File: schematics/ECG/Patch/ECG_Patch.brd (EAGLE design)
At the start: 27.3 x 27.3 mm, 7 parts

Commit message: changed 4 pin to through hole and added v1.0 marking
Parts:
- removed U$1: M80-4SMT, harwin:M80-4_SMT
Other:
- board text added: "ECG Patch v1.0"
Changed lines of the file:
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@@
 <setting verticaltext="up"/>
 </settings>
-<grid distance="1" unitdist="mil" unit="mil" style="lines" multiple="1" display="no" altdistance="0.025" altunitdist="inch" altunit="inch"/>
+<grid distance="0.001" unitdist="inch" unit="inch" style="lines" multiple="1" display="yes" altdistance="0.025" altunitdist="inch" altunit="inch"/>
 <layers>
 <layer number="1" name="Top" color="4" fill="1" visible="yes" active="yes"/>
@@
 <wire x1="27.305" y1="27.305" x2="0" y2="27.305" width="0" layer="20"/>
 <wire x1="0" y1="27.305" x2="0" y2="0" width="0" layer="20"/>
-<circle x="26.797" y="13.208" radius="0.08031875" width="0.4064" layer="21"/>
+<circle x="21.4122" y="13.2588" radius="0.508" width="0.4064" layer="22"/>
+<text x="22.8092" y="26.3652" size="0.4064" layer="21">ECG Patch v1.0</text>
 </plain>
 <attributes>
@@
 </autorouter>
 <elements>
-<element name="CONN1" library="harwin" package="M80-4-V" value="M80-4V" x="2.667" y="13.2588"/>
 <element name="CONN2" library="harwin" package="M80-6-V" value="M80-6V" x="24.638" y="13.2588" rot="R90"/>
 <element name="LL" library="testpad" package="TP20R" value="TPTP20R" x="22.86" y="8.001" rot="MR270">
@@
 <attribute name="TP_SIGNAL_NAME" value="" x="18.5674" y="18.542" size="1.778" layer="28" rot="MR270" display="off"/>
 </element>
-<element name="U$1" library="harwin" package="M80-4_SMT" value="M80-4SMT" x="11.8618" y="13.2842" rot="R90"/>
+<element name="CONN1" library="harwin" package="M80-4-V" value="M80-4V" x="2.667" y="13.2588"/>
 </elements>
 <signals>

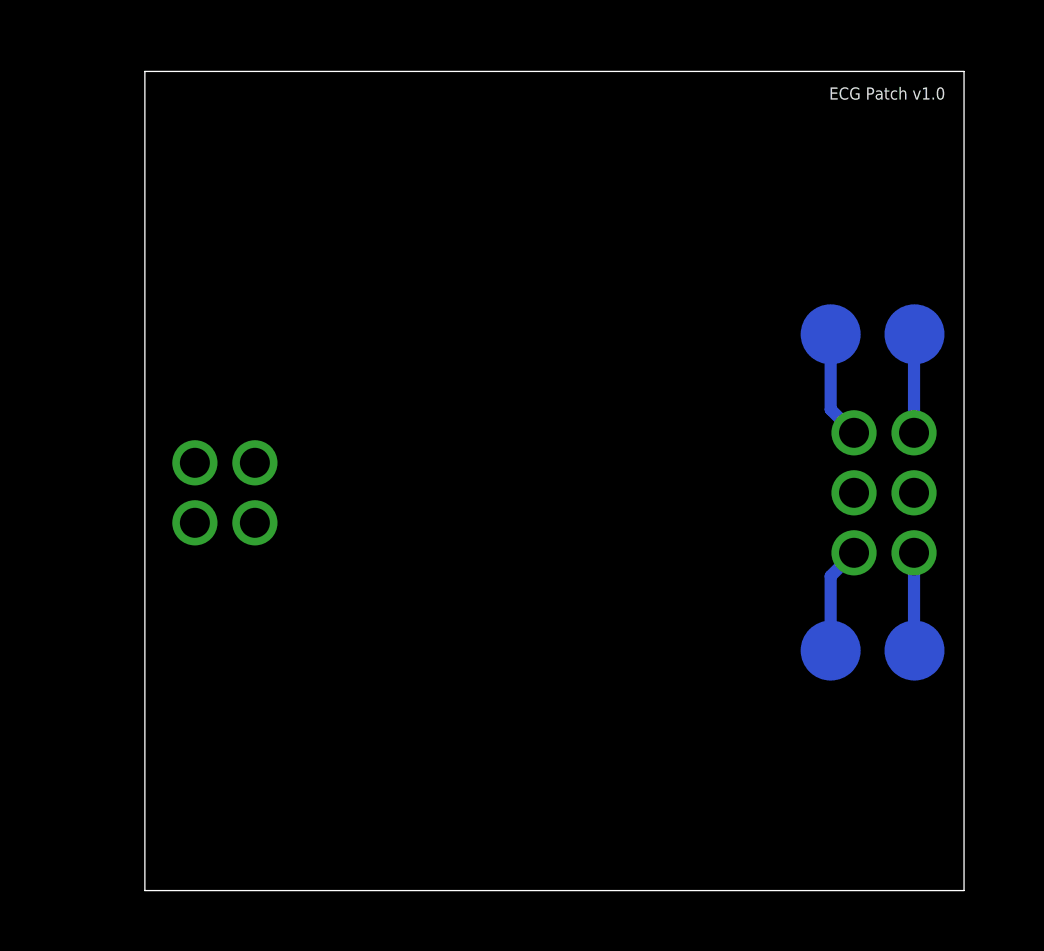
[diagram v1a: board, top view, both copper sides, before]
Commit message: switched ECG boards to spring loaded pin headers
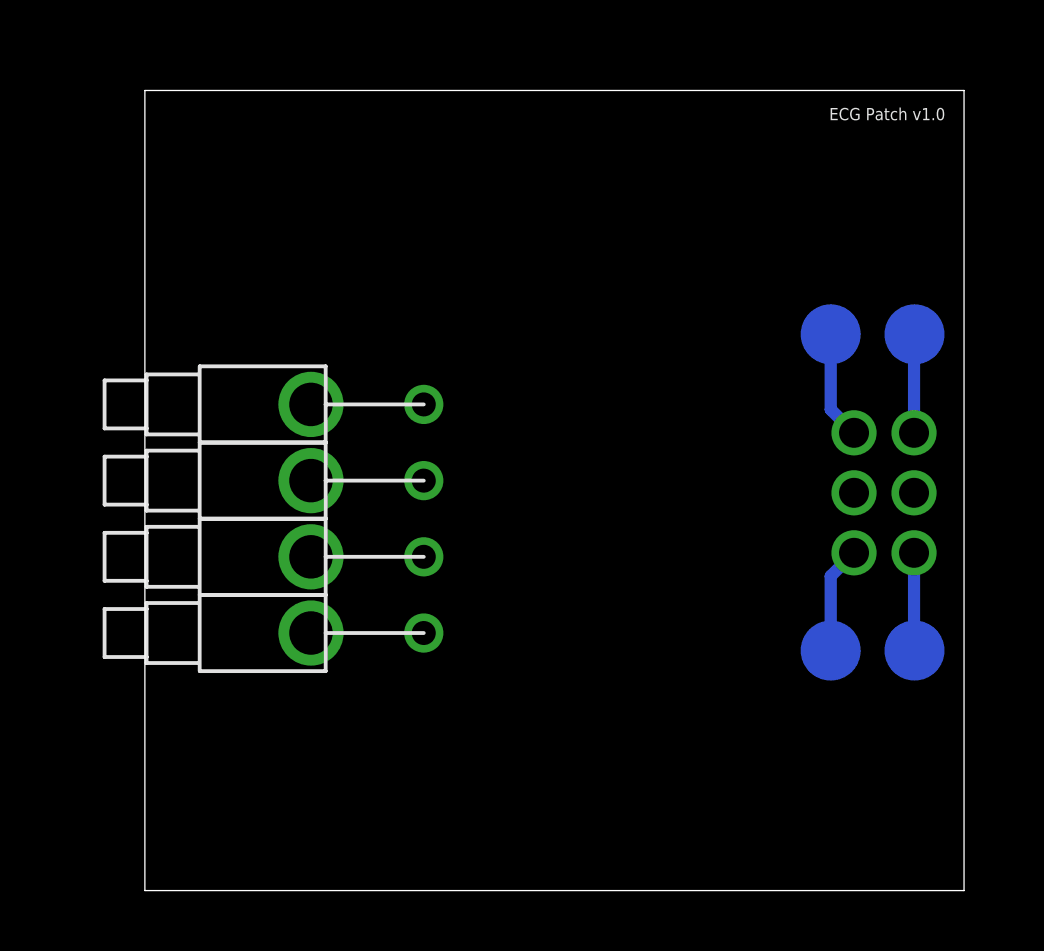
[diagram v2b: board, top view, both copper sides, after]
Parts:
- removed CONN1: M80-4V, harwin:M80-4-V
- added U$1, U$2, U$3, U$4: PISTON_RA_TH, pins:PISTON_RA_TH
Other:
- board size 27.3 x 27.3 mm -> 27.3 x 26.7 mm
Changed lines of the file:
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@@
 <?xml version="1.0" encoding="utf-8"?>
 <!DOCTYPE eagle SYSTEM "eagle.dtd">
-<eagle version="6.4">
+<eagle version="6.5.0">
 <drawing>
 <settings>
@@
 <plain>
 <wire x1="0" y1="0" x2="27.305" y2="0" width="0" layer="20"/>
-<wire x1="27.305" y1="0" x2="27.305" y2="27.305" width="0" layer="20"/>
-<wire x1="27.305" y1="27.305" x2="0" y2="27.305" width="0" layer="20"/>
-<wire x1="0" y1="27.305" x2="0" y2="0" width="0" layer="20"/>
+<wire x1="27.305" y1="0" x2="27.305" y2="26.67" width="0" layer="20"/>
+<wire x1="27.305" y1="26.67" x2="0" y2="26.67" width="0" layer="20"/>
+<wire x1="0" y1="26.67" x2="0" y2="0" width="0" layer="20"/>
 <circle x="21.4122" y="13.2588" radius="0.508" width="0.4064" layer="22"/>
-<text x="22.8092" y="26.3652" size="0.4064" layer="21">ECG Patch v1.0</text>
+<text x="22.8092" y="25.6794" size="0.4064" layer="21">ECG Patch v1.0</text>
 </plain>
 <attributes>
@@
 <attribute name="TP_SIGNAL_NAME" value="" x="18.5674" y="18.542" size="1.778" layer="28" rot="MR270" display="off"/>
 </element>
-<element name="CONN1" library="harwin" package="M80-4-V" value="M80-4V" x="2.667" y="13.2588"/>
+<element name="U$1" library="pins" package="PISTON_RA_TH" value="PISTON_RA_TH" x="9.2964" y="16.2052" rot="R180"/>
+<element name="U$2" library="pins" package="PISTON_RA_TH" value="PISTON_RA_TH" x="9.2964" y="13.6652" rot="R180"/>
+<element name="U$3" library="pins" package="PISTON_RA_TH" value="PISTON_RA_TH" x="9.2964" y="11.1252" rot="R180"/>
+<element name="U$4" library="pins" package="PISTON_RA_TH" value="PISTON_RA_TH" x="9.2964" y="8.5852" rot="R180"/>
 </elements>
 <signals>

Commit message: redesigned patch board and charging board
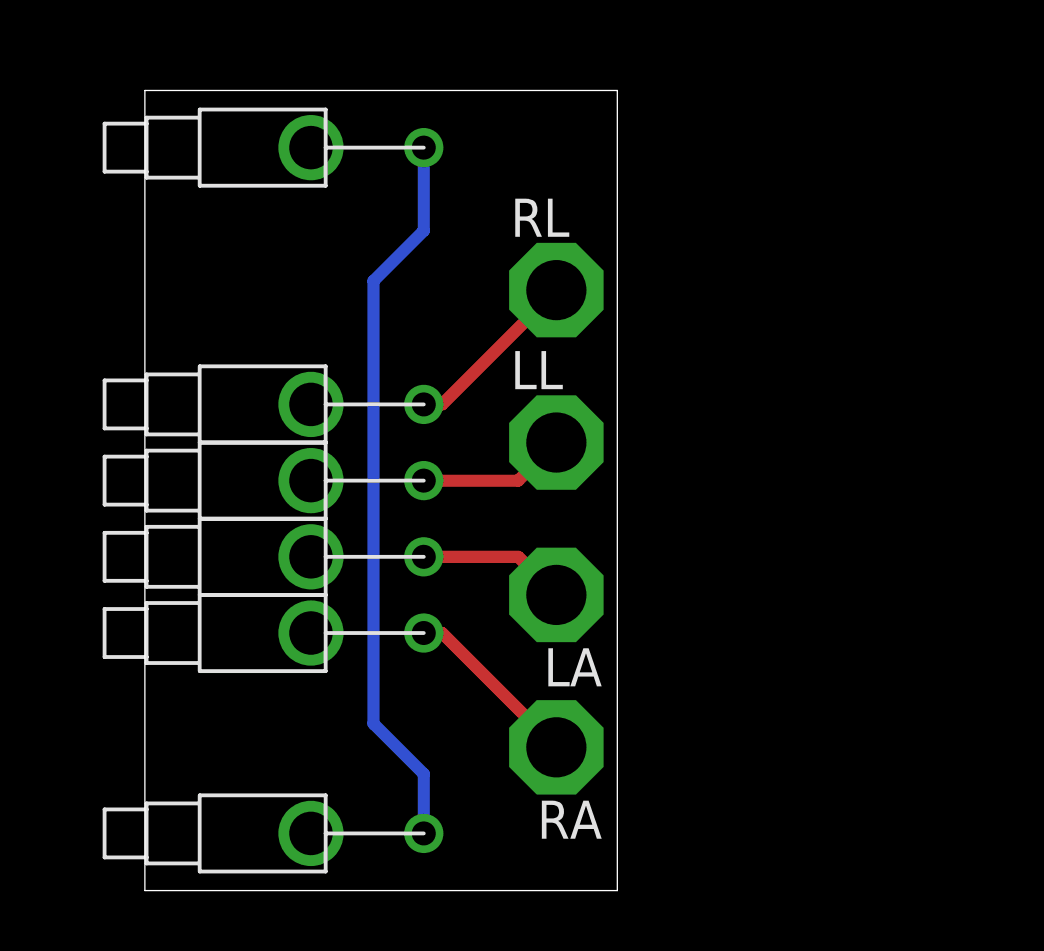
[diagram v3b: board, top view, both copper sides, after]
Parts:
- removed CONN2: M80-6V, harwin:M80-6-V
- added U$5, U$6: PISTON_RA_TH, pins:PISTON_RA_TH
- LA, LL, RA, RL: value TPTP20R -> TPSQPAD1-20; device testpad:TP20R -> testpad:P1-20
- moved RA 18.2 mm to (13.7, 4.78), flipped to the top, turned to 180 degrees
- moved LA 12.1 mm to (13.7, 9.86), flipped to the top
- moved LL 11.5 mm to (13.7, 14.9), flipped to the top, turned to 0 degrees
- moved RL 9.26 mm to (13.7, 20.0), flipped to the top, turned to 0 degrees
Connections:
- removed net LA: CONN2.1, LA.TP
- removed net LL: CONN2.6, LL.TP
- removed net RA: CONN2.3, RA.TP
- removed net RL: CONN2.4, RL.TP
- new net BATT: U$5.1, U$6.1
- new net N$1: LL.TP, U$2.1
- new net N$2: RL.TP, U$1.1
- new net N$3: LA.TP, U$3.1
- new net N$4: RA.TP, U$4.1
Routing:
- net BATT: track 0.00 -> 24.2 mm
- net N$4: track 0.00 -> 6.00 mm
- net N$2: track 0.00 -> 6.00 mm
- net N$3: track 0.00 -> 4.95 mm
- net N$1: track 0.00 -> 4.95 mm
- net RL: track 3.61 -> 0.00 mm
- net LL: track 3.58 -> 0.00 mm
- net RA: track 3.29 -> 0.00 mm
- net LA: track 3.26 -> 0.00 mm
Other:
- board size 27.3 x 26.7 mm -> 15.7 x 26.7 mm
- board text removed: "ECG Patch v1.0"
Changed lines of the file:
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@@
 <setting verticaltext="up"/>
 </settings>
-<grid distance="0.001" unitdist="inch" unit="inch" style="lines" multiple="1" display="yes" altdistance="0.025" altunitdist="inch" altunit="inch"/>
+<grid distance="0.001" unitdist="inch" unit="mil" style="lines" multiple="1" display="yes" altdistance="0.025" altunitdist="inch" altunit="inch"/>
 <layers>
 <layer number="1" name="Top" color="4" fill="1" visible="yes" active="yes"/>
-<layer number="2" name="Route2" color="1" fill="3" visible="no" active="yes"/>
+<layer number="2" name="Route2" color="1" fill="3" visible="no" active="no"/>
 <layer number="3" name="Route3" color="4" fill="3" visible="no" active="no"/>
 <layer number="14" name="Route14" color="1" fill="6" visible="no" active="no"/>
-<layer number="15" name="Route15" color="4" fill="6" visible="no" active="yes"/>
+<layer number="15" name="Route15" color="4" fill="6" visible="no" active="no"/>
 <layer number="16" name="Bottom" color="1" fill="1" visible="yes" active="yes"/>
 <layer number="17" name="Pads" color="2" fill="1" visible="yes" active="yes"/>
@@
 <board>
 <plain>
-<wire x1="0" y1="0" x2="27.305" y2="0" width="0" layer="20"/>
-<wire x1="27.305" y1="0" x2="27.305" y2="26.67" width="0" layer="20"/>
-<wire x1="27.305" y1="26.67" x2="0" y2="26.67" width="0" layer="20"/>
+<wire x1="0" y1="0" x2="15.748" y2="0" width="0" layer="20"/>
+<wire x1="15.748" y1="0" x2="15.748" y2="26.67" width="0" layer="20"/>
+<wire x1="15.748" y1="26.67" x2="0" y2="26.67" width="0" layer="20"/>
 <wire x1="0" y1="26.67" x2="0" y2="0" width="0" layer="20"/>
-<circle x="21.4122" y="13.2588" radius="0.508" width="0.4064" layer="22"/>
-<text x="22.8092" y="25.6794" size="0.4064" layer="21">ECG Patch v1.0</text>
 </plain>
 <attributes>
@@
 necessary adjustments and save your customized
 design rules under a new name.</description>
-<param name="layerSetup" value="(1*2+15*16)"/>
+<param name="layerSetup" value="(1*16)"/>
 <param name="mtCopper" value="0.035mm 0.035mm 0.035mm 0.035mm 0.035mm 0.035mm 0.035mm 0.035mm 0.035mm 0.035mm 0.035mm 0.035mm 0.035mm 0.035mm 0.035mm 0.035mm"/>
 <param name="mtIsolate" value="0.5mm 0.5mm 0.2mm 0.15mm 0.2mm 0.15mm 0.2mm 0.15mm 0.2mm 0.15mm 0.2mm 0.15mm 0.2mm 0.15mm 0.5mm"/>
@@
 </autorouter>
 <elements>
-<element name="CONN2" library="harwin" package="M80-6-V" value="M80-6V" x="24.638" y="13.2588" rot="R90"/>
-<element name="LL" library="testpad" package="TP20R" value="TPTP20R" x="22.86" y="8.001" rot="MR270">
-<attribute name="TP_SIGNAL_NAME" value="" x="22.86" y="8.001" size="1.778" layer="28" rot="MR270" display="off"/>
-</element>
-<element name="LA" library="testpad" package="TP20R" value="TPTP20R" x="25.654" y="8.001" rot="MR180">
-<attribute name="TP_SIGNAL_NAME" value="" x="25.654" y="8.001" size="1.778" layer="28" rot="MR180" display="off"/>
-</element>
-<element name="RA" library="testpad" package="TP20R" value="TPTP20R" x="25.654" y="18.542" rot="MR0">
-<attribute name="TP_SIGNAL_NAME" value="" x="25.654" y="18.542" size="1.778" layer="28" rot="MR0" display="off"/>
-</element>
-<element name="RL" library="testpad" package="TP20R" value="TPTP20R" x="22.86" y="18.542" rot="MR270">
-<attribute name="TP_SIGNAL_NAME" value="" x="18.5674" y="18.542" size="1.778" layer="28" rot="MR270" display="off"/>
-</element>
 <element name="U$1" library="pins" package="PISTON_RA_TH" value="PISTON_RA_TH" x="9.2964" y="16.2052" rot="R180"/>
 <element name="U$2" library="pins" package="PISTON_RA_TH" value="PISTON_RA_TH" x="9.2964" y="13.6652" rot="R180"/>
 <element name="U$3" library="pins" package="PISTON_RA_TH" value="PISTON_RA_TH" x="9.2964" y="11.1252" rot="R180"/>
 <element name="U$4" library="pins" package="PISTON_RA_TH" value="PISTON_RA_TH" x="9.2964" y="8.5852" rot="R180"/>
+<element name="LL" library="testpad" package="P1-20" value="TPSQPAD1-20" x="13.716" y="14.9352">
+<attribute name="TP_SIGNAL_NAME" value="" x="13.716" y="14.9352" size="1.778" layer="27" display="off"/>
+</element>
+<element name="RL" library="testpad" package="P1-20" value="TPSQPAD1-20" x="13.716" y="20.0152">
+<attribute name="TP_SIGNAL_NAME" value="" x="13.716" y="20.0152" size="1.778" layer="27" display="off"/>
+</element>
+<element name="LA" library="testpad" package="P1-20" value="TPSQPAD1-20" x="13.716" y="9.8552" rot="R180">
+<attribute name="TP_SIGNAL_NAME" value="" x="13.716" y="9.8552" size="1.778" layer="27" rot="R180" display="off"/>
+</element>
+<element name="RA" library="testpad" package="P1-20" value="TPSQPAD1-20" x="13.716" y="4.7752" rot="R180">
+<attribute name="TP_SIGNAL_NAME" value="" x="13.716" y="4.7752" size="1.778" layer="27" rot="R180" display="off"/>
+</element>
+<element name="U$5" library="pins" package="PISTON_RA_TH" value="PISTON_RA_TH" x="9.2964" y="24.765" rot="R180"/>
+<element name="U$6" library="pins" package="PISTON_RA_TH" value="PISTON_RA_TH" x="9.2964" y="1.905" rot="R180"/>
 </elements>
 <signals>
-<signal name="LA">
-<contactref element="CONN2" pad="1"/>
+<signal name="N$1">
+<contactref element="U$2" pad="1"/>
+<contactref element="LL" pad="TP"/>
+<wire x1="9.2964" y1="13.6652" x2="12.446" y2="13.6652" width="0.4064" layer="1"/>
+<wire x1="12.446" y1="13.6652" x2="13.716" y2="14.9352" width="0.4064" layer="1"/>
+</signal>
+<signal name="N$2">
+<contactref element="U$1" pad="1"/>
+<contactref element="RL" pad="TP"/>
+<wire x1="9.2964" y1="16.2052" x2="9.906" y2="16.2052" width="0.4064" layer="1"/>
+<wire x1="9.906" y1="16.2052" x2="13.716" y2="20.0152" width="0.4064" layer="1"/>
+</signal>
+<signal name="N$3">
+<contactref element="U$3" pad="1"/>
 <contactref element="LA" pad="TP"/>
-<wire x1="25.638" y1="11.2588" x2="25.638" y2="8.017" width="0.4064" layer="16"/>
-<wire x1="25.638" y1="8.017" x2="25.654" y2="8.001" width="0.4064" layer="16"/>
-</signal>
-<signal name="RL">
-<contactref element="RL" pad="TP"/>
-<contactref element="CONN2" pad="4"/>
-<wire x1="22.86" y1="18.542" x2="22.86" y2="16.0368" width="0.4064" layer="16"/>
-<wire x1="22.86" y1="16.0368" x2="23.638" y2="15.2588" width="0.4064" layer="16"/>
-</signal>
-<signal name="LL">
-<contactref element="CONN2" pad="6"/>
-<contactref element="LL" pad="TP"/>
-<wire x1="22.86" y1="8.001" x2="22.86" y2="10.4808" width="0.4064" layer="16"/>
-<wire x1="22.86" y1="10.4808" x2="23.638" y2="11.2588" width="0.4064" layer="16"/>
-</signal>
-<signal name="RA">
+<wire x1="9.2964" y1="11.1252" x2="12.446" y2="11.1252" width="0.4064" layer="1"/>
+<wire x1="12.446" y1="11.1252" x2="13.716" y2="9.8552" width="0.4064" layer="1"/>
+</signal>
+<signal name="N$4">
+<contactref element="U$4" pad="1"/>
 <contactref element="RA" pad="TP"/>
-<contactref element="CONN2" pad="3"/>
-<wire x1="25.638" y1="15.2588" x2="25.638" y2="18.526" width="0.4064" layer="16"/>
-<wire x1="25.638" y1="18.526" x2="25.654" y2="18.542" width="0.4064" layer="16"/>
+<wire x1="9.2964" y1="8.5852" x2="9.906" y2="8.5852" width="0.4064" layer="1"/>
+<wire x1="9.906" y1="8.5852" x2="13.716" y2="4.7752" width="0.4064" layer="1"/>
+</signal>
+<signal name="BATT">
+<contactref element="U$5" pad="1"/>
+<contactref element="U$6" pad="1"/>
+<wire x1="9.2964" y1="24.765" x2="9.2964" y2="21.9964" width="0.4064" layer="16"/>
+<wire x1="9.2964" y1="21.9964" x2="7.62" y2="20.32" width="0.4064" layer="16"/>
+<wire x1="7.62" y1="20.32" x2="7.62" y2="5.5626" width="0.4064" layer="16"/>
+<wire x1="7.62" y1="5.5626" x2="9.2964" y2="3.8862" width="0.4064" layer="16"/>
+<wire x1="9.2964" y1="3.8862" x2="9.2964" y2="1.905" width="0.4064" layer="16"/>
 </signal>
 </signals>
